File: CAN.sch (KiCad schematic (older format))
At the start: 9 parts

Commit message: corrected CAN schematic
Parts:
- removed JP?: Jumper_NC_Small, Connector_PinHeader_2.54mm:PinHeader_1x02_P2.54mm_Vertical, symbol Device:Jumper_NC_Small
- removed R?: 120, Resistor_SMD:R_0805_2012Metric, symbol Device:R
- added C15: 4.7nF, Capacitor_SMD:C_0603_1608Metric, symbol Device:C
- added JP4, JP5: SolderJumper_2_Open, symbol Jumper:SolderJumper_2_Open
- C16, C17: renamed from C?; value 86pF -> 100pF; footprint Capacitor_SMD:C_0805_2012Metric -> Capacitor_SMD:C_0603_1608Metric; Description (none) -> 100pF ±10% 50V X7R 0603 Multilayer Ceramic Capacitors; Manufacturer (none) -> Samsung Electro-Mechanics; Mount (none) -> MOUNT; MountType (none) -> SMD; PartNumber (none) -> CL10B101KB8NNNC
- D6: renamed from D?; Description (none) -> Bidirectional 12V 13.3V 31V 19A (8/20us) SOT-23(SOT-23-3) T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; Manufacturer (none) -> Littelfuse; Mount (none) -> MOUNT; MountType (none) -> SMD; PartNumber (none) -> SM712-02HTG
- FL1: renamed from FL?; Description (none) -> Signal Line 2.8kΩ @ 10MHz 51uH @ 100kHz 1Ω 50V 4532 Common 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; Manufacturer (none) -> TDK; Mount (none) -> MOUNT; MountType (none) -> SMD; PartNumber (none) -> ACT45B-510-2P-TL003
- R18, R19: renamed from R?; value 100 -> 60.4; Manufacturer (none) -> -; Mount (none) -> MOUNT; MountType (none) -> SMD
- U4: renamed from U?; value TJA1051T -> TJA1051T-3; symbol Interface_CAN_LIN:TJA1051T -> Interface_CAN_LIN:TJA1051T-3; Description (none) -> Transceiver CAN 1/1 5Mbps SOIC-8_150mil CAN ICs RoHS; Manufacturer (none) -> NXP; Mount (none) -> MOUNT; MountType (none) -> SMD; PartNumber (none) -> TJA1051T/3/1J
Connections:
- net CAN_H: now also C17.1
- net CAN_L: now also C16.1
- net GND: now also C15.2
- net at FL1.1, U4.7 (CANH): now also JP5.1 (A); no longer R19.1
- net at R19.2: now also R18.2, C15.1; no longer C16.1
- net at FL1.2, U4.6 (CANL): now also JP4.1 (A); no longer R18.1
- net MCU_VDD: now reaches U4.5 (VIO)
- new net: JP5.2 (B), R19.1
- new net: JP4.2 (B), R18.1
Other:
- moved on the sheet: C21, C22, D9, FL2, R22, R23

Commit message: Start routing
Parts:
- JP4, JP5: footprint (none) -> Jumper:SolderJumper-2_P1.3mm_Open_RoundedPad1.0x1.5mm
- R18, R19: Description (none) -> 60.4Ω ±1% 0.1W ±100ppm/℃ 0603 Chip Resistor - Surface Mount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; Manufacturer - -> YAGEO; PartNumber (none) -> RC0603FR-0760R4L
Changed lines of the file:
@@
 F 1 "60.4" H 4920 4855 50  0000 L CNN
 F 2 "Resistor_SMD:R_0805_2012Metric" V 4780 4900 50  0001 C CNN
-F 3 "~" H 4850 4900 50  0001 C CNN
+F 3 "https://datasheet.lcsc.com/szlcsc/YAGEO-RC0603FR-0760R4L_C245987.pdf" H 4850 4900 50  0001 C CNN
 F 4 "MOUNT" H 4850 4900 50  0001 C CNN "Mount"
 F 5 "SMD" H 4850 4900 50  0001 C CNN "MountType"
-F 6 "-" H 4850 4900 50  0001 C CNN "Manufacturer"
+F 6 "YAGEO" H 4850 4900 50  0001 C CNN "Manufacturer"
+F 7 "60.4Ω ±1% 0.1W ±100ppm/℃ 0603 Chip Resistor - Surface Mount RoHS" H 4850 4900 50  0001 C CNN "Description"
+F 8 "RC0603FR-0760R4L" H 4850 4900 50  0001 C CNN "PartNumber"
 	1    4850 4900
 	1    0    0    -1
@@
 F 1 "60.4" H 4470 4855 50  0000 L CNN
 F 2 "Resistor_SMD:R_0805_2012Metric" V 4330 4900 50  0001 C CNN
-F 3 "~" H 4400 4900 50  0001 C CNN
+F 3 "https://datasheet.lcsc.com/szlcsc/YAGEO-RC0603FR-0760R4L_C245987.pdf" H 4400 4900 50  0001 C CNN
 F 4 "MOUNT" H 4400 4900 50  0001 C CNN "Mount"
 F 5 "SMD" H 4400 4900 50  0001 C CNN "MountType"
-F 6 "-" H 4400 4900 50  0001 C CNN "Manufacturer"
+F 6 "YAGEO" H 4400 4900 50  0001 C CNN "Manufacturer"
+F 7 "60.4Ω ±1% 0.1W ±100ppm/℃ 0603 Chip Resistor - Surface Mount RoHS" H 4400 4900 50  0001 C CNN "Description"
+F 8 "RC0603FR-0760R4L" H 4400 4900 50  0001 C CNN "PartNumber"
 	1    4400 4900
 	1    0    0    -1
@@
 F 0 "JP9" V 4400 4568 50  0000 L CNN
 F 1 "SolderJumper_2_Open" V 4445 4568 50  0001 L CNN
-F 2 "" H 4400 4500 50  0001 C CNN
+F 2 "Jumper:SolderJumper-2_P1.3mm_Open_RoundedPad1.0x1.5mm" H 4400 4500 50  0001 C CNN
 F 3 "NOT A COMPONENT" H 4400 4500 50  0001 C CNN
 F 4 "NOT A COMPONENT" H 4400 4500 50  0001 C CNN "Description"
@@
 F 0 "JP10" V 4850 4568 50  0000 L CNN
 F 1 "SolderJumper_2_Open" V 4895 4568 50  0001 L CNN
-F 2 "" H 4850 4500 50  0001 C CNN
+F 2 "Jumper:SolderJumper-2_P1.3mm_Open_RoundedPad1.0x1.5mm" H 4850 4500 50  0001 C CNN
 F 3 "NOT A COMPONENT" H 4850 4500 50  0001 C CNN
 F 4 "NOT A COMPONENT" H 4850 4500 50  0001 C CNN "Description"

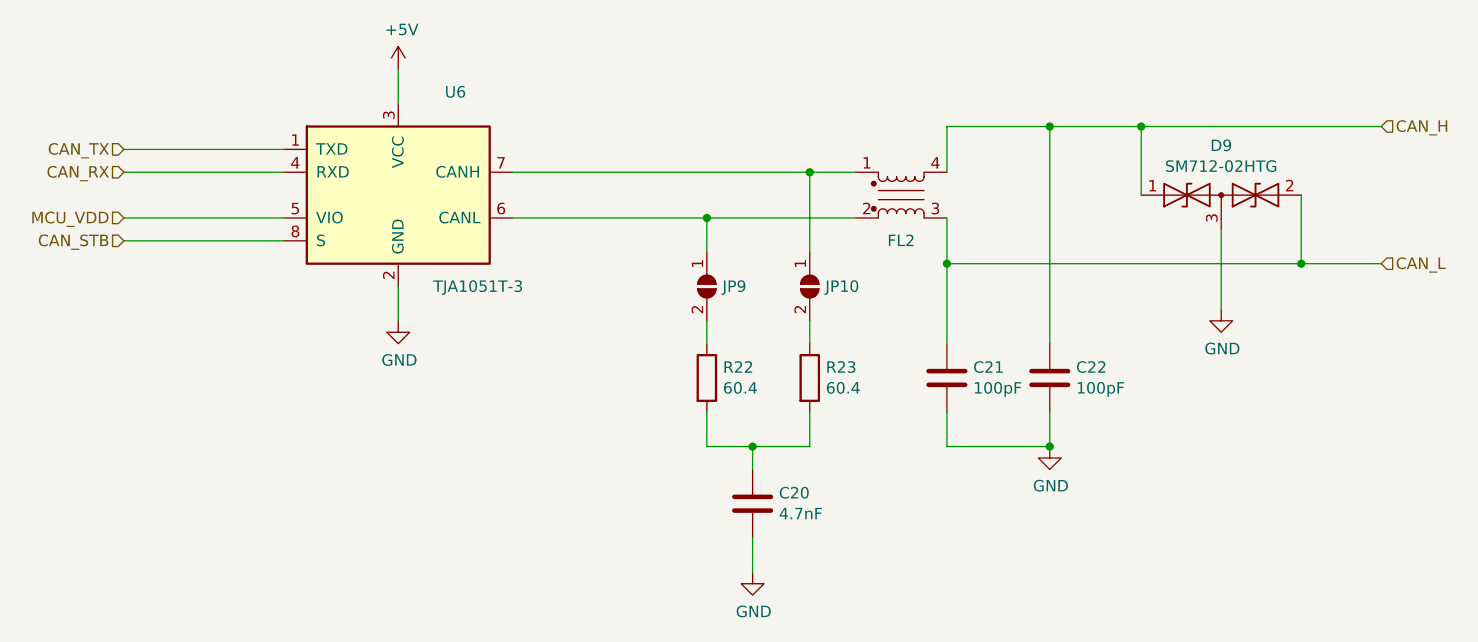
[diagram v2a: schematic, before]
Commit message: CAN part routing
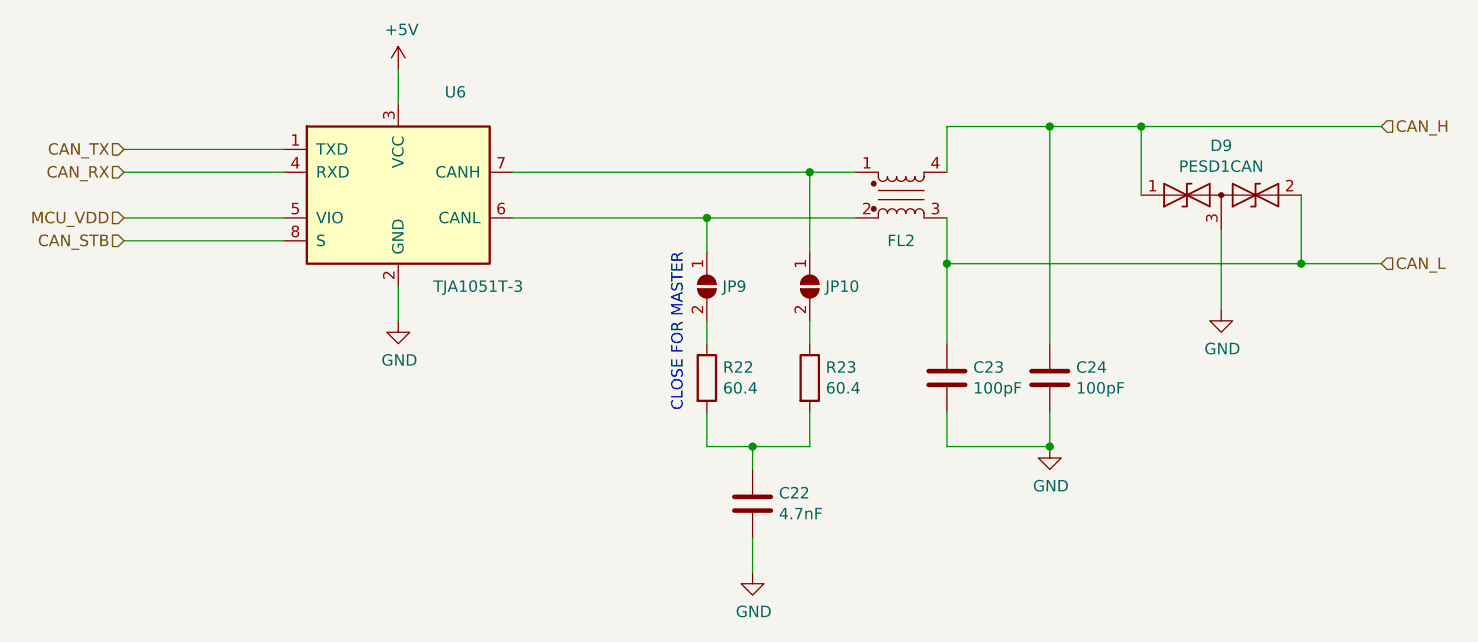
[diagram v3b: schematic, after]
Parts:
- D6: value SM712-02HTG -> PESD1CAN; Description Bidirectional 12V 13.3V 31V 19A (8/20us) SOT-23(SOT-23-3) T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 -> Bidirectional 24V 25.4V 70V 3A SOT-23(SOT-23-3) Diodes - ES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; Manufacturer Littelfuse -> Nexperia; PartNumber SM712-02HTG -> PESD1CAN,215
- renumbered C15 to C16, C16 to C17, C17 to C18
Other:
- note added: "CLOSE FOR MASTER"
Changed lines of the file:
@@
 AR Path="/5DE444CB/60085282" Ref="#PWR?"  Part="1"
 AR Path="/5DFCEA89/60085282" Ref="#PWR?"  Part="1"
-AR Path="/60084F77/60085282" Ref="#PWR033"  Part="1"
+AR Path="/60084F77/60085282" Ref="#PWR034"  Part="1"
 AR Path="/60085B71/60085282" Ref="#PWR?"  Part="1"
-AR Path="/600FAE10/60085282" Ref="#PWR040"  Part="1"
-F 0 "#PWR040" H 6650 4350 50  0001 C CNN
+AR Path="/600FAE10/60085282" Ref="#PWR042"  Part="1"
+F 0 "#PWR042" H 6650 4350 50  0001 C CNN
 F 1 "GND" H 6655 4427 50  0000 C CNN
 F 2 "" H 6650 4600 50  0001 C CNN
@@
 AR Path="/5DE444CB/60085283" Ref="#PWR?"  Part="1"
 AR Path="/5DFCEA89/60085283" Ref="#PWR?"  Part="1"
-AR Path="/60084F77/60085283" Ref="#PWR030"  Part="1"
+AR Path="/60084F77/60085283" Ref="#PWR031"  Part="1"
 AR Path="/60085B71/60085283" Ref="#PWR?"  Part="1"
-AR Path="/600FAE10/60085283" Ref="#PWR037"  Part="1"
-F 0 "#PWR037" H 3050 4400 50  0001 C CNN
+AR Path="/600FAE10/60085283" Ref="#PWR039"  Part="1"
+F 0 "#PWR039" H 3050 4400 50  0001 C CNN
 F 1 "GND" H 3055 4477 50  0000 C CNN
 F 2 "" H 3050 4650 50  0001 C CNN
@@
 AR Path="/5DE444CB/5DFA8A6B" Ref="#PWR?"  Part="1"
 AR Path="/5DFCEA89/5DFA8A6B" Ref="#PWR?"  Part="1"
-AR Path="/60084F77/5DFA8A6B" Ref="#PWR029"  Part="1"
+AR Path="/60084F77/5DFA8A6B" Ref="#PWR030"  Part="1"
 AR Path="/60085B71/5DFA8A6B" Ref="#PWR?"  Part="1"
-AR Path="/600FAE10/5DFA8A6B" Ref="#PWR036"  Part="1"
-F 0 "#PWR036" H 3050 3400 50  0001 C CNN
+AR Path="/600FAE10/5DFA8A6B" Ref="#PWR038"  Part="1"
+F 0 "#PWR038" H 3050 3400 50  0001 C CNN
 F 1 "+5V" H 3065 3723 50  0000 C CNN
 F 2 "" H 3050 3550 50  0001 C CNN
@@
 AR Path="/600FAE10/5DFB4268" Ref="D9"  Part="1"
 F 0 "D9" H 6650 4316 50  0000 C CNN
-F 1 "SM712-02HTG" H 6650 4225 50  0000 C CNN
+F 1 "PESD1CAN" H 6650 4225 50  0000 C CNN
 F 2 "Package_TO_SOT_SMD:SOT-23" H 6500 4100 50  0001 C CNN
-F 3 "https://m.littelfuse.com/~/media/electronics/datasheets/tvs_diode_arrays/littelfuse_tvs_diode_array_sm712_datasheet.pdf.pdf" H 6500 4100 50  0001 C CNN
+F 3 "https://datasheet.lcsc.com/szlcsc/Nexperia-PESD1CAN-215_C15771.pdf" H 6500 4100 50  0001 C CNN
 F 4 "MOUNT" H 6650 4100 50  0001 C CNN "Mount"
 F 5 "SMD" H 6650 4100 50  0001 C CNN "MountType"
-F 6 "Littelfuse" H 6650 4100 50  0001 C CNN "Manufacturer"
-F 7 "SM712-02HTG" H 6650 4100 50  0001 C CNN "PartNumber"
-F 8 "Bidirectional 12V 13.3V 31V 19A (8/20us) SOT-23(SOT-23-3) TVS RoHS" H 6650 4100 50  0001 C CNN "Description"
+F 6 "Nexperia" H 6650 4100 50  0001 C CNN "Manufacturer"
+F 7 "PESD1CAN,215 " H 6650 4100 50  0001 C CNN "PartNumber"
+F 8 "Bidirectional 24V 25.4V 70V 3A SOT-23(SOT-23-3) Diodes - ESD RoHS" H 6650 4100 50  0001 C CNN "Description"
 	1    6650 4100
 	1    0    0    -1
@@
 AR Path="/5DE444CB/60085289" Ref="C?"  Part="1"
 AR Path="/5DFCEA89/60085289" Ref="C?"  Part="1"
-AR Path="/60084F77/60085289" Ref="C16"  Part="1"
+AR Path="/60084F77/60085289" Ref="C17"  Part="1"
 AR Path="/60085B71/60085289" Ref="C?"  Part="1"
-AR Path="/600FAE10/60085289" Ref="C21"  Part="1"
-F 0 "C21" H 5565 4946 50  0000 L CNN
+AR Path="/600FAE10/60085289" Ref="C23"  Part="1"
+F 0 "C23" H 5565 4946 50  0000 L CNN
 F 1 "100pF" H 5565 4855 50  0000 L CNN
 F 2 "Capacitor_SMD:C_0603_1608Metric" H 5488 4750 50  0001 C CNN
@@
 AR Path="/5DE444CB/6008528A" Ref="C?"  Part="1"
 AR Path="/5DFCEA89/6008528A" Ref="C?"  Part="1"
-AR Path="/60084F77/6008528A" Ref="C17"  Part="1"
+AR Path="/60084F77/6008528A" Ref="C18"  Part="1"
 AR Path="/60085B71/6008528A" Ref="C?"  Part="1"
-AR Path="/600FAE10/6008528A" Ref="C22"  Part="1"
-F 0 "C22" H 6015 4946 50  0000 L CNN
+AR Path="/600FAE10/6008528A" Ref="C24"  Part="1"
+F 0 "C24" H 6015 4946 50  0000 L CNN
 F 1 "100pF" H 6015 4855 50  0000 L CNN
 F 2 "Capacitor_SMD:C_0603_1608Metric" H 5938 4750 50  0001 C CNN
@@
 AR Path="/5DE444CB/6008528B" Ref="#PWR?"  Part="1"
 AR Path="/5DFCEA89/6008528B" Ref="#PWR?"  Part="1"
-AR Path="/60084F77/6008528B" Ref="#PWR032"  Part="1"
+AR Path="/60084F77/6008528B" Ref="#PWR033"  Part="1"
 AR Path="/60085B71/6008528B" Ref="#PWR?"  Part="1"
-AR Path="/600FAE10/6008528B" Ref="#PWR039"  Part="1"
-F 0 "#PWR039" H 5900 4950 50  0001 C CNN
+AR Path="/600FAE10/6008528B" Ref="#PWR041"  Part="1"
+F 0 "#PWR041" H 5900 4950 50  0001 C CNN
 F 1 "GND" H 5905 5027 50  0000 C CNN
 F 2 "" H 5900 5200 50  0001 C CNN
@@
 AR Path="/5DE444CB/600EDC46" Ref="C?"  Part="1"
 AR Path="/5DFCEA89/600EDC46" Ref="C?"  Part="1"
-AR Path="/60084F77/600EDC46" Ref="C15"  Part="1"
+AR Path="/60084F77/600EDC46" Ref="C16"  Part="1"
 AR Path="/60085B71/600EDC46" Ref="C?"  Part="1"
-AR Path="/600FAE10/600EDC46" Ref="C20"  Part="1"
-F 0 "C20" H 4715 5496 50  0000 L CNN
+AR Path="/600FAE10/600EDC46" Ref="C22"  Part="1"
+F 0 "C22" H 4715 5496 50  0000 L CNN
 F 1 "4.7nF" H 4715 5405 50  0000 L CNN
 F 2 "Capacitor_SMD:C_0603_1608Metric" H 4638 5300 50  0001 C CNN
@@
 AR Path="/5DE444CB/60107433" Ref="#PWR?"  Part="1"
 AR Path="/5DFCEA89/60107433" Ref="#PWR?"  Part="1"
-AR Path="/60084F77/60107433" Ref="#PWR031"  Part="1"
+AR Path="/60084F77/60107433" Ref="#PWR032"  Part="1"
 AR Path="/60085B71/60107433" Ref="#PWR?"  Part="1"
-AR Path="/600FAE10/60107433" Ref="#PWR038"  Part="1"
-F 0 "#PWR038" H 4600 5500 50  0001 C CNN
+AR Path="/600FAE10/60107433" Ref="#PWR040"  Part="1"
+F 0 "#PWR040" H 4600 5500 50  0001 C CNN
 F 1 "GND" H 4605 5577 50  0000 C CNN
 F 2 "" H 4600 5750 50  0001 C CNN
@@
 Wire Wire Line
 	4600 5600 4600 5750
+Text Notes 4300 5050 1    50   ~ 0
+CLOSE FOR MASTER
 $EndSCHEMATC
